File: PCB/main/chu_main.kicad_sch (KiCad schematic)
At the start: 83 parts, among them K1 Conn_01x01_Female, K10 Conn_01x01_Female, K11 Conn_01x01_Female, K12 Conn_01x01_Female, K13 Conn_01x01_Female, K14 Conn_01x01_Female, K15 Conn_01x01_Female, K16 Conn_01x01_Female, K17 Conn_01x01_Female, K18 Conn_01x01_Female, K19 Conn_01x01_Female, K2 Conn_01x01_Female, K20 Conn_01x01_Female, K21 Conn_01x01_Female, K22 Conn_01x01_Female, K23 Conn_01x01_Female, K24 Conn_01x01_Female, K25 Conn_01x01_Female, K26 Conn_01x01_Female, K27 Conn_01x01_Female, K28 Conn_01x01_Female, K29 Conn_01x01_Female, K3 Conn_01x01_Female, K30 Conn_01x01_Female, K31 Conn_01x01_Female, K32 Conn_01x01_Female, K4 Conn_01x01_Female, K5 Conn_01x01_Female, K6 Conn_01x01_Female, K7 Conn_01x01_Female, K8 Conn_01x01_Female, K9 Conn_01x01_Female, U1 Pico, U3 MPR121QR2_BOARD, U4 MPR121QR2_BOARD, U5 MPR121QR2_BOARD, U8 SN74LV1T34DBV

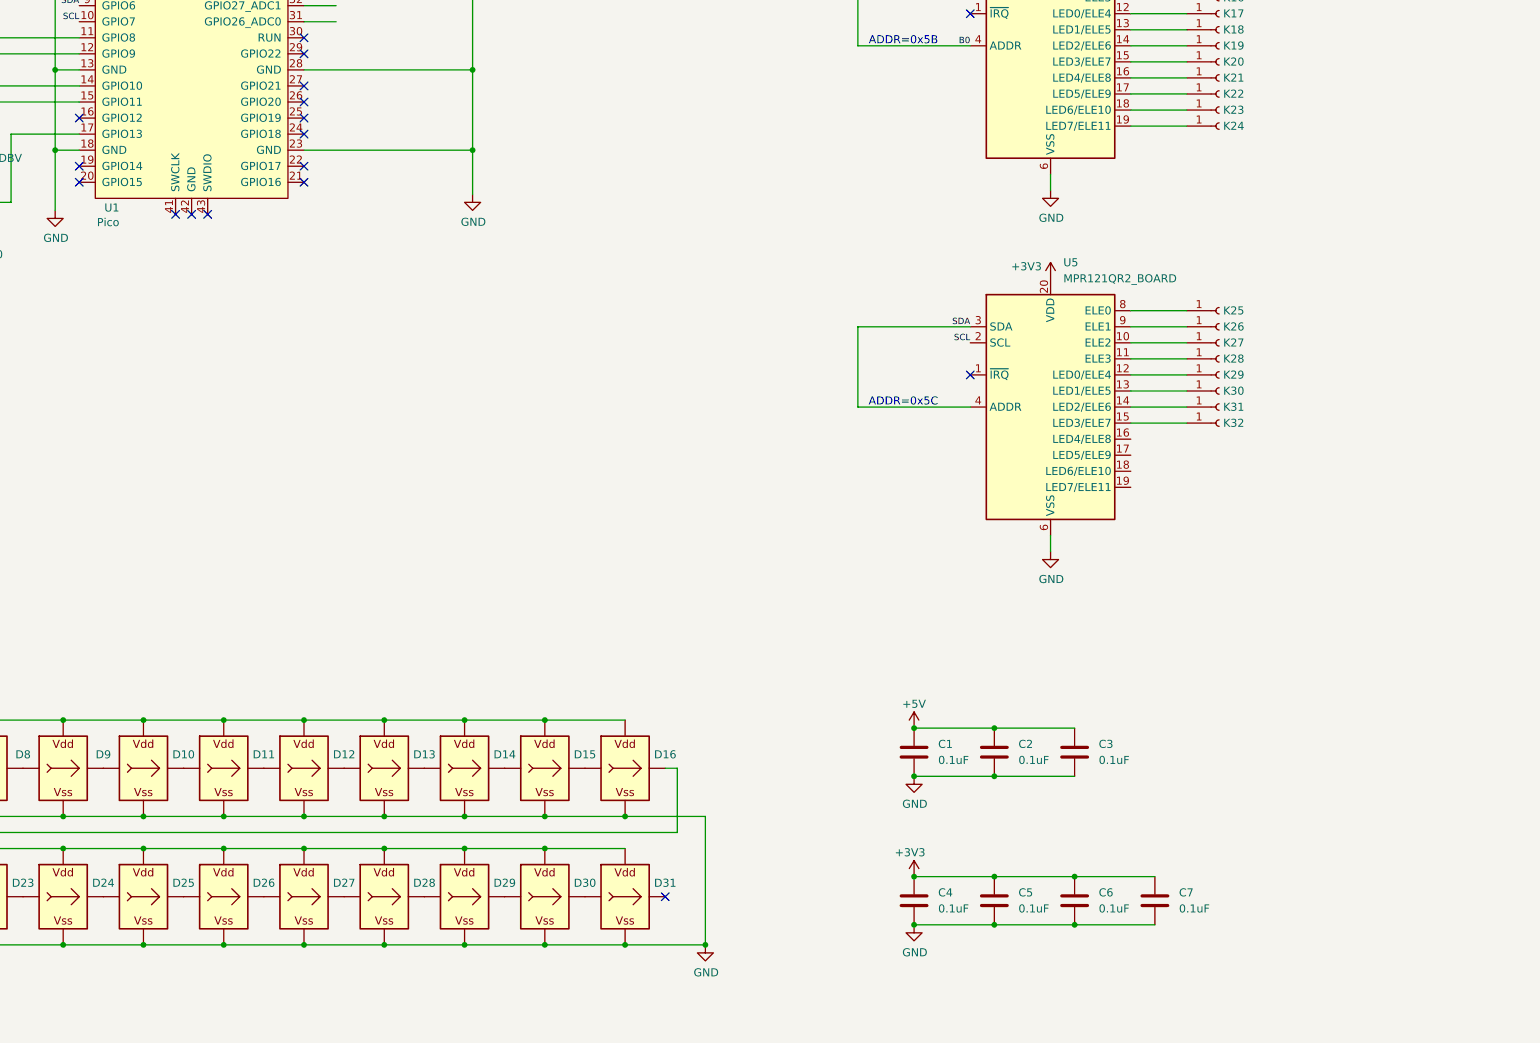
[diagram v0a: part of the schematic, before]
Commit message: Some updates (keypad, IR sensor firmware)
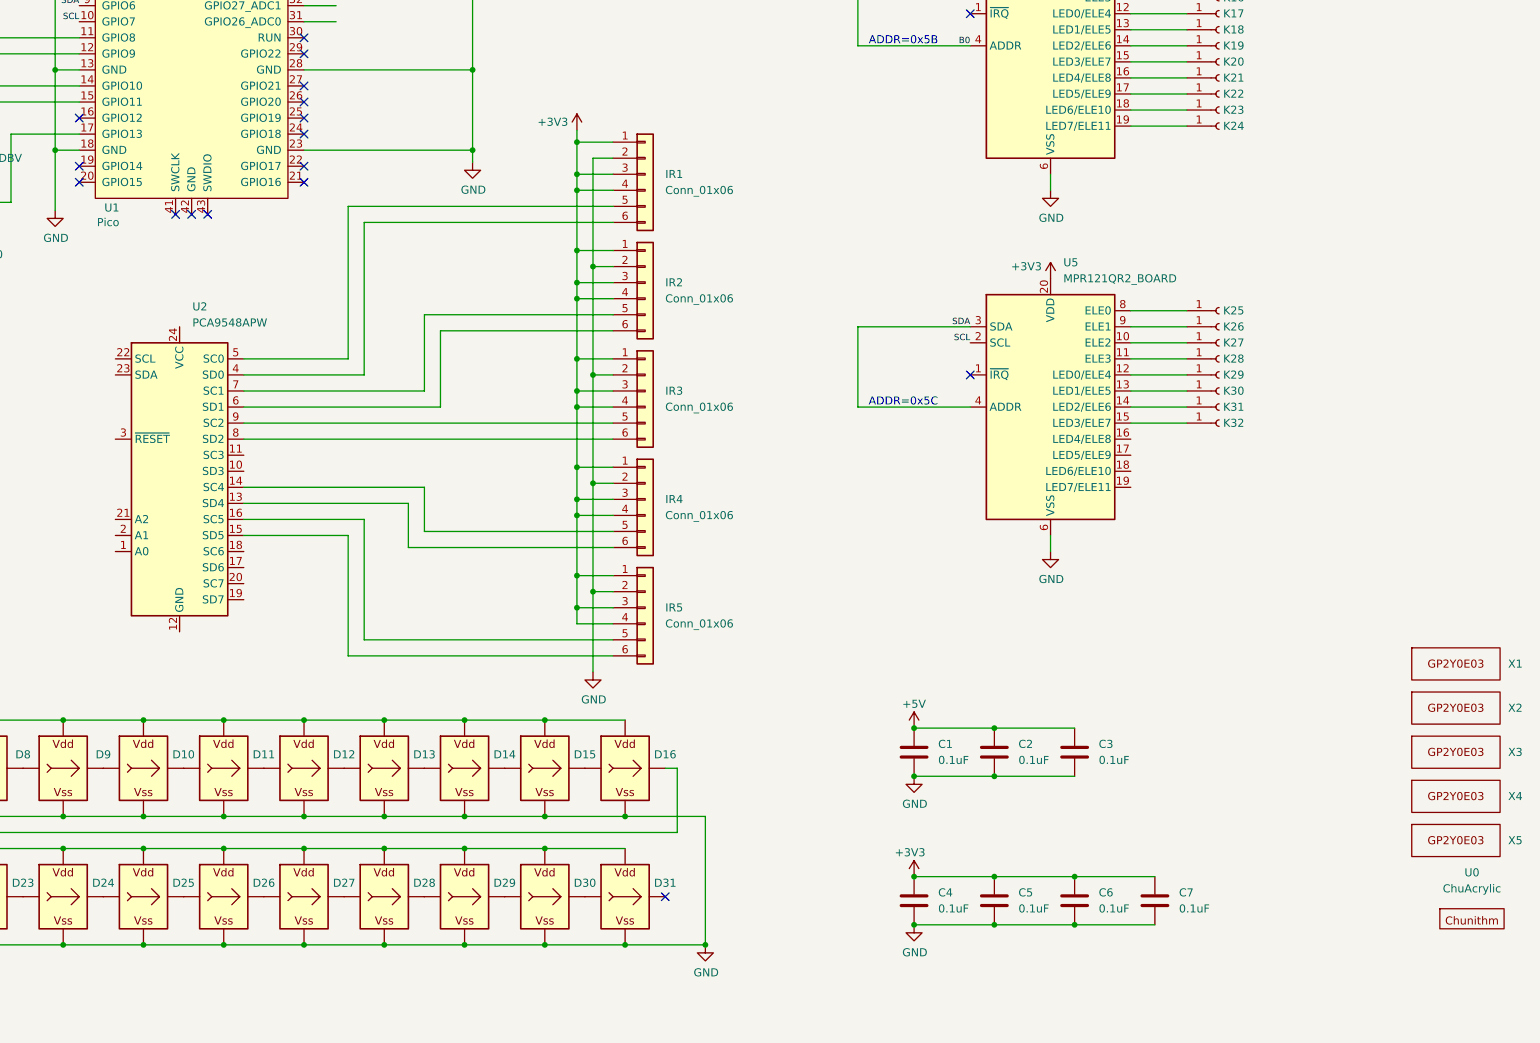
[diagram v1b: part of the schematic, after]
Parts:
- added IR1, IR2, IR3, IR4, IR5: Conn_01x06, chu_main:GP2Y0E03, symbol Connector_Generic:Conn_01x06
- added U0: ChuAcrylic, chu_main:ChuAcrylic, symbol chu_main:ChuAcrylic
- added U2: PCA9548APW, Package_SO:TSSOP-24_4.4x7.8mm_P0.65mm, symbol Interface_Expansion:PCA9548APW
- added X1, X2, X3, X4, X5: GP2Y0E03_REAL, chu_main:GP2Y0E03_REAL, symbol chu_main:GP2Y0E03_REAL
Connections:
- net +3V3: now also IR1.1 (Pin_1), IR1.3 (Pin_3), IR1.4 (Pin_4), IR2.1 (Pin_1), IR2.3 (Pin_3), IR2.4 (Pin_4), IR3.1 (Pin_1), IR3.3 (Pin_3), IR3.4 (Pin_4), IR4.1 (Pin_1), IR4.3 (Pin_3), IR4.4 (Pin_4), IR5.1 (Pin_1), IR5.3 (Pin_3), IR5.4 (Pin_4)
- net GND: now also IR1.2 (Pin_2), IR2.2 (Pin_2), IR3.2 (Pin_2), IR4.2 (Pin_2), IR5.2 (Pin_2)
- new net: IR4.5 (Pin_5), U2.14 (SC4)
- new net: IR4.6 (Pin_6), U2.13 (SD4)
- new net: IR1.5 (Pin_5), U2.5 (SC0)
- new net: IR1.6 (Pin_6), U2.4 (SD0)
- new net: IR2.5 (Pin_5), U2.7 (SC1)
- new net: IR2.6 (Pin_6), U2.6 (SD1)
- new net: IR3.5 (Pin_5), U2.9 (SC2)
- new net: IR3.6 (Pin_6), U2.8 (SD2)
- new net: IR5.5 (Pin_5), U2.16 (SC5)
- new net: IR5.6 (Pin_6), U2.15 (SD5)

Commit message: Layout progress 40%
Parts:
- added D32, D33, D34, D35, D36: WS2812B_Unified, chu_main:WS2812B-2835, symbol chu_main:WS2812B_Unified
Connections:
- net +5V: now also D32.V (VDD), D33.V (VDD), D34.V (VDD), D35.V (VDD), D36.V (VDD)
- net GND: now also D32.G (VSS), D33.G (VSS), D34.G (VSS), D35.G (VSS), D36.G (VSS)
- net at D31.O (Out): now also D32.I (In)
- new net: D32.O (Out), D33.I (In)
- new net: D34.O (Out), D35.I (In)
- new net: D35.O (Out), D36.I (In)
- new net: D33.O (Out), D34.I (In)

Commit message: Layoug progress 70%
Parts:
- added R10, R11, R12, R13, R4, R5, R6, R7, R8, R9: 4.7K, Resistor_SMD:R_0603_1608Metric, symbol Device:R_Small
- U1: footprint chu_main:RPi_Pico_SMD_Pins -> chu_main:RPi_Pico_SMD_Pins_Strip
- renumbered R20 to R1, R21 to R2, R4 to R3
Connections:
- net +3V3: now also U2.24 (VCC), R10.2, R11.2, R12.2, R13.2, R4.2, R5.2, R6.2, R7.2, R8.2, R9.2
- net GND: now also U2.1 (A0), U2.12 (GND), U2.2 (A1), U2.21 (A2)
- net SCL: now also U1.22 (GPIO17), U2.22 (SCL); no longer U1.10 (GPIO7)
- net SDA: now also U1.21 (GPIO16), U2.23 (SDA); no longer U1.9 (GPIO6)
- net at R3.2, U8.2 (A): now also U1.4 (GPIO2); no longer U1.17 (GPIO13)
- net at U1.25 (GPIO19): now also U2.3 (~{RESET})
- net SCL_2: now reaches U2.14 (SC4)
- net SCL_2: now also IR2.5 (Pin_5), R6.1; no longer IR4.5 (Pin_5)
- net SDA_2: now reaches U2.13 (SD4)
- net SDA_2: now also IR2.6 (Pin_6), R7.1; no longer IR4.6 (Pin_6)
- net SCL_1: now reaches IR1.5 (Pin_5)
- net SCL_1: now also U2.16 (SC5), R4.1; no longer U2.5 (SC0)
- net SDA_1: now reaches IR1.6 (Pin_6)
- net SDA_1: now also U2.15 (SD5), R5.1; no longer U2.4 (SD0)
- net SCL_5: now reaches U2.7 (SC1)
- net SCL_5: now also IR5.5 (Pin_5), R12.1; no longer IR2.5 (Pin_5)
- net SDA_5: now reaches U2.6 (SD1)
- net SDA_5: now also IR5.6 (Pin_6), R13.1; no longer IR2.6 (Pin_6)
- net SCL_3: now reaches IR3.5 (Pin_5)
- net SCL_3: now also U2.5 (SC0), R8.1; no longer U2.9 (SC2)
- net SDA_3: now reaches IR3.6 (Pin_6)
- net SDA_3: now also U2.4 (SD0), R9.1; no longer U2.8 (SD2)
- new net SCL_4: IR4.5 (Pin_5), R10.1, U2.9 (SC2)
- new net SDA_4: IR4.6 (Pin_6), R11.1, U2.8 (SD2)
- no-connect marks 25 -> 41
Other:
- moved on the sheet: IR1, IR2, IR3, IR4, IR5, R3, U1, U8

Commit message: PCB v1 done
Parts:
- added C6: 0.1uF, Capacitor_SMD:C_0603_1608Metric_Pad1.08x0.95mm_HandSolder, symbol Device:C
- renumbered C6 to C8
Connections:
- net B0 is gone; now on net +3V3: U4.4 (ADDR)
- net +3V3: no longer C4.1, C5.1, C7.1
- net +5V: now also C4.1, C5.1, C7.1, C6.1
- net GND: now also C6.2
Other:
- moved on the sheet: C1, C2, C3, C4, C5, C8

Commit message: PCB v1.1 (LED footprint update)
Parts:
- D32, D33, D34, D35, D36: footprint chu_main:WS2812B-2835 -> chu_main:WS2812B-4020
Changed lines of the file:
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@@
       (effects (font (size 1.27 1.27)) hide)
     )
-    (property "Footprint" "chu_main:WS2812B-2835" (id 2) (at 83.82 269.24 0)
+    (property "Footprint" "chu_main:WS2812B-4020" (id 2) (at 83.82 269.24 0)
       (effects (font (size 1.27 1.27)) (justify left top) hide)
     )
@@
       (effects (font (size 1.27 1.27)) hide)
     )
-    (property "Footprint" "chu_main:WS2812B-2835" (id 2) (at 121.92 269.24 0)
+    (property "Footprint" "chu_main:WS2812B-4020" (id 2) (at 121.92 269.24 0)
       (effects (font (size 1.27 1.27)) (justify left top) hide)
     )
@@
       (effects (font (size 1.27 1.27)) hide)
     )
-    (property "Footprint" "chu_main:WS2812B-2835" (id 2) (at 109.22 269.24 0)
+    (property "Footprint" "chu_main:WS2812B-4020" (id 2) (at 109.22 269.24 0)
       (effects (font (size 1.27 1.27)) (justify left top) hide)
     )
@@
       (effects (font (size 1.27 1.27)) hide)
     )
-    (property "Footprint" "chu_main:WS2812B-2835" (id 2) (at 96.52 269.24 0)
+    (property "Footprint" "chu_main:WS2812B-4020" (id 2) (at 96.52 269.24 0)
       (effects (font (size 1.27 1.27)) (justify left top) hide)
     )
@@
       (effects (font (size 1.27 1.27)) hide)
     )
-    (property "Footprint" "chu_main:WS2812B-2835" (id 2) (at 134.62 269.24 0)
+    (property "Footprint" "chu_main:WS2812B-4020" (id 2) (at 134.62 269.24 0)
       (effects (font (size 1.27 1.27)) (justify left top) hide)
     )
@@
     )
     (path "/0601a6ad-0bb7-4dea-8b69-576e319947e8"
-      (reference "D32") (unit 1) (value "WS2812B_Unified") (footprint "chu_main:WS2812B-2835")
+      (reference "D32") (unit 1) (value "WS2812B_Unified") (footprint "chu_main:WS2812B-4020")
     )
     (path "/748713f3-186a-410a-9525-4caea40c2977"
-      (reference "D33") (unit 1) (value "WS2812B_Unified") (footprint "chu_main:WS2812B-2835")
+      (reference "D33") (unit 1) (value "WS2812B_Unified") (footprint "chu_main:WS2812B-4020")
     )
     (path "/6dae0991-cb3e-47fa-a605-c2da04657d64"
-      (reference "D34") (unit 1) (value "WS2812B_Unified") (footprint "chu_main:WS2812B-2835")
+      (reference "D34") (unit 1) (value "WS2812B_Unified") (footprint "chu_main:WS2812B-4020")
     )
     (path "/22b824d1-9964-4065-ad53-8a225029207b"
-      (reference "D35") (unit 1) (value "WS2812B_Unified") (footprint "chu_main:WS2812B-2835")
+      (reference "D35") (unit 1) (value "WS2812B_Unified") (footprint "chu_main:WS2812B-4020")
     )
     (path "/f9638a2d-254e-4d1b-82c0-7c7b0aa8cf89"
-      (reference "D36") (unit 1) (value "WS2812B_Unified") (footprint "chu_main:WS2812B-2835")
+      (reference "D36") (unit 1) (value "WS2812B_Unified") (footprint "chu_main:WS2812B-4020")
     )
     (path "/5da28692-0cd4-4544-9250-22252cbda908"

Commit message: Finetune PCB and CAD files
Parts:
- K10, K12, K14, K16, K18, K2, K20, K22, K24, K26, K28, K30, K32, K4, K6, K8: footprint chu_main:ChuKeyScrews -> chu_main:ChuKey
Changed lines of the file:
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@@
       (effects (font (size 1.27 1.27)) (justify left) hide)
     )
-    (property "Footprint" "chu_main:ChuKeyScrews" (id 2) (at 354.33 162.56 0)
+    (property "Footprint" "chu_main:ChuKey" (id 2) (at 354.33 162.56 0)
       (effects (font (size 1.27 1.27)) hide)
     )
@@
       (effects (font (size 1.27 1.27)) (justify left) hide)
     )
-    (property "Footprint" "chu_main:ChuKeyScrews" (id 2) (at 354.33 90.17 0)
+    (property "Footprint" "chu_main:ChuKey" (id 2) (at 354.33 90.17 0)
       (effects (font (size 1.27 1.27)) hide)
     )
@@
       (effects (font (size 1.27 1.27)) (justify left) hide)
     )
-    (property "Footprint" "chu_main:ChuKeyScrews" (id 2) (at 354.33 157.48 0)
+    (property "Footprint" "chu_main:ChuKey" (id 2) (at 354.33 157.48 0)
       (effects (font (size 1.27 1.27)) hide)
     )
@@
       (effects (font (size 1.27 1.27)) (justify left) hide)
     )
-    (property "Footprint" "chu_main:ChuKeyScrews" (id 2) (at 354.33 43.18 0)
+    (property "Footprint" "chu_main:ChuKey" (id 2) (at 354.33 43.18 0)
       (effects (font (size 1.27 1.27)) hide)
     )
@@
       (effects (font (size 1.27 1.27)) (justify left) hide)
     )
-    (property "Footprint" "chu_main:ChuKeyScrews" (id 2) (at 354.33 53.34 0)
+    (property "Footprint" "chu_main:ChuKey" (id 2) (at 354.33 53.34 0)
       (effects (font (size 1.27 1.27)) hide)
     )
@@
       (effects (font (size 1.27 1.27)) (justify left) hide)
     )
-    (property "Footprint" "chu_main:ChuKeyScrews" (id 2) (at 354.33 105.41 0)
+    (property "Footprint" "chu_main:ChuKey" (id 2) (at 354.33 105.41 0)
       (effects (font (size 1.27 1.27)) hide)
     )
@@
       (effects (font (size 1.27 1.27)) (justify left) hide)
     )
-    (property "Footprint" "chu_main:ChuKeyScrews" (id 2) (at 354.33 110.49 0)
+    (property "Footprint" "chu_main:ChuKey" (id 2) (at 354.33 110.49 0)
       (effects (font (size 1.27 1.27)) hide)
     )
@@
       (effects (font (size 1.27 1.27)) (justify left) hide)
     )
-    (property "Footprint" "chu_main:ChuKeyScrews" (id 2) (at 354.33 95.25 0)
+    (property "Footprint" "chu_main:ChuKey" (id 2) (at 354.33 95.25 0)
       (effects (font (size 1.27 1.27)) hide)
     )
@@
       (effects (font (size 1.27 1.27)) (justify left) hide)
     )
-    (property "Footprint" "chu_main:ChuKeyScrews" (id 2) (at 354.33 115.57 0)
+    (property "Footprint" "chu_main:ChuKey" (id 2) (at 354.33 115.57 0)
       (effects (font (size 1.27 1.27)) hide)
     )
@@
       (effects (font (size 1.27 1.27)) (justify left) hide)
     )
-    (property "Footprint" "chu_main:ChuKeyScrews" (id 2) (at 354.33 147.32 0)
+    (property "Footprint" "chu_main:ChuKey" (id 2) (at 354.33 147.32 0)
       (effects (font (size 1.27 1.27)) hide)
     )
@@
       (effects (font (size 1.27 1.27)) (justify left) hide)
     )
-    (property "Footprint" "chu_main:ChuKeyScrews" (id 2) (at 354.33 48.26 0)
+    (property "Footprint" "chu_main:ChuKey" (id 2) (at 354.33 48.26 0)
       (effects (font (size 1.27 1.27)) hide)
     )
@@
       (effects (font (size 1.27 1.27)) (justify left) hide)
     )
-    (property "Footprint" "chu_main:ChuKeyScrews" (id 2) (at 354.33 58.42 0)
+    (property "Footprint" "chu_main:ChuKey" (id 2) (at 354.33 58.42 0)
       (effects (font (size 1.27 1.27)) hide)
     )
@@
       (effects (font (size 1.27 1.27)) (justify left) hide)
     )
-    (property "Footprint" "chu_main:ChuKeyScrews" (id 2) (at 354.33 38.1 0)
+    (property "Footprint" "chu_main:ChuKey" (id 2) (at 354.33 38.1 0)
       (effects (font (size 1.27 1.27)) hide)
     )
@@
       (effects (font (size 1.27 1.27)) (justify left) hide)
     )
-    (property "Footprint" "chu_main:ChuKeyScrews" (id 2) (at 354.33 152.4 0)
+    (property "Footprint" "chu_main:ChuKey" (id 2) (at 354.33 152.4 0)
       (effects (font (size 1.27 1.27)) hide)
     )
@@
       (effects (font (size 1.27 1.27)) (justify left) hide)
     )
-    (property "Footprint" "chu_main:ChuKeyScrews" (id 2) (at 354.33 33.02 0)
+    (property "Footprint" "chu_main:ChuKey" (id 2) (at 354.33 33.02 0)
       (effects (font (size 1.27 1.27)) hide)
     )
@@
       (effects (font (size 1.27 1.27)) (justify left) hide)
     )
-    (property "Footprint" "chu_main:ChuKeyScrews" (id 2) (at 354.33 100.33 0)
+    (property "Footprint" "chu_main:ChuKey" (id 2) (at 354.33 100.33 0)
       (effects (font (size 1.27 1.27)) hide)
     )
@@
     )
     (path "/f9c41c5b-098b-4d5a-9976-ba6515a2ec7a"
-      (reference "K2") (unit 1) (value "Conn_01x01_Female") (footprint "chu_main:ChuKeyScrews")
+      (reference "K2") (unit 1) (value "Conn_01x01_Female") (footprint "chu_main:ChuKey")
     )
     (path "/08d85abb-3237-4d72-99f4-57092b02965c"
@@
     )
     (path "/df2d39c2-3ca5-4c87-97fa-12314841d0a0"
-      (reference "K4") (unit 1) (value "Conn_01x01_Female") (footprint "chu_main:ChuKeyScrews")
+      (reference "K4") (unit 1) (value "Conn_01x01_Female") (footprint "chu_main:ChuKey")
     )
     (path "/6ecbd99d-c2ce-4143-a99b-e8bcd2a7a013"
@@
     )
     (path "/4d878ce4-aae5-4362-b40c-c0ea29c8c9a4"
-      (reference "K6") (unit 1) (value "Conn_01x01_Female") (footprint "chu_main:ChuKeyScrews")
+      (reference "K6") (unit 1) (value "Conn_01x01_Female") (footprint "chu_main:ChuKey")
     )
     (path "/282b3b7f-4888-4ba1-8e3e-f750677d4343"
@@
     )
     (path "/c72f957e-5817-4166-8b43-d130f38d215d"
-      (reference "K8") (unit 1) (value "Conn_01x01_Female") (footprint "chu_main:ChuKeyScrews")
+      (reference "K8") (unit 1) (value "Conn_01x01_Female") (footprint "chu_main:ChuKey")
     )
     (path "/8eded052-2713-4c3d-8ebb-70994d2a49eb"
@@
     )
     (path "/79a4aff7-a5e2-4b7e-bb09-cf0dd022f771"
-      (reference "K10") (unit 1) (value "Conn_01x01_Female") (footprint "chu_main:ChuKeyScrews")
+      (reference "K10") (unit 1) (value "Conn_01x01_Female") (footprint "chu_main:ChuKey")
     )
     (path "/0563fcc7-e713-4f2d-9e87-2634364fb680"
@@
     )
     (path "/db4705d9-b3d2-49a4-96f3-33f3ee5db3c5"
-      (reference "K12") (unit 1) (value "Conn_01x01_Female") (footprint "chu_main:ChuKeyScrews")
+      (reference "K12") (unit 1) (value "Conn_01x01_Female") (footprint "chu_main:ChuKey")
     )
     (path "/fdd4bd59-1d65-42a6-b5bf-d786dc261db6"
@@
     )
     (path "/1cc33a48-faf2-4585-867a-a271a201d1c5"
-      (reference "K14") (unit 1) (value "Conn_01x01_Female") (footprint "chu_main:ChuKeyScrews")
+      (reference "K14") (unit 1) (value "Conn_01x01_Female") (footprint "chu_main:ChuKey")
     )
     (path "/551e7bff-6472-460c-adbb-2baecd766975"
@@
     )
     (path "/a6efa1f1-0c09-4f74-9948-95d685f056fa"
-      (reference "K16") (unit 1) (value "Conn_01x01_Female") (footprint "chu_main:ChuKeyScrews")
+      (reference "K16") (unit 1) (value "Conn_01x01_Female") (footprint "chu_main:ChuKey")
     )
     (path "/7fcaf0bc-9ab1-4c53-91fc-cd181af52a2c"
@@
     )
     (path "/fb2d01ff-dfa5-4ffd-b72f-0ed114023612"
-      (reference "K18") (unit 1) (value "Conn_01x01_Female") (footprint "chu_main:ChuKeyScrews")
+      (reference "K18") (unit 1) (value "Conn_01x01_Female") (footprint "chu_main:ChuKey")
     )
     (path "/47a29468-d763-49d8-a905-041dfd2b0fdb"
@@
     )
     (path "/8324a555-6f53-4c15-aa91-91ec35339cac"
-      (reference "K20") (unit 1) (value "Conn_01x01_Female") (footprint "chu_main:ChuKeyScrews")
+      (reference "K20") (unit 1) (value "Conn_01x01_Female") (footprint "chu_main:ChuKey")
     )
     (path "/f7103f9a-bdc4-45f5-add5-83a57c590782"
@@
     )
     (path "/9ac68718-a1f9-42bb-ab42-ac43d3637d9a"
-      (reference "K22") (unit 1) (value "Conn_01x01_Female") (footprint "chu_main:ChuKeyScrews")
+      (reference "K22") (unit 1) (value "Conn_01x01_Female") (footprint "chu_main:ChuKey")
     )
     (path "/70b72b6d-13c0-49b6-9606-488d841a2a1e"
@@
     )
     (path "/ae98f63d-97f8-4350-916b-711df88aa422"
-      (reference "K24") (unit 1) (value "Conn_01x01_Female") (footprint "chu_main:ChuKeyScrews")
+      (reference "K24") (unit 1) (value "Conn_01x01_Female") (footprint "chu_main:ChuKey")
     )
     (path "/9dffab08-f394-41c2-8837-8cc9e3f1bf44"
@@
     )
     (path "/bed81a25-aad1-400c-b41d-73f476c42ab9"
-      (reference "K26") (unit 1) (value "Conn_01x01_Female") (footprint "chu_main:ChuKeyScrews")
+      (reference "K26") (unit 1) (value "Conn_01x01_Female") (footprint "chu_main:ChuKey")
     )
     (path "/40517cf5-e968-448a-8be5-e06b125a310d"
@@
     )
     (path "/f5feeb96-188a-4208-8596-e178a6729411"
-      (reference "K28") (unit 1) (value "Conn_01x01_Female") (footprint "chu_main:ChuKeyScrews")
+      (reference "K28") (unit 1) (value "Conn_01x01_Female") (footprint "chu_main:ChuKey")
     )
     (path "/1d6a95ed-c55c-4902-989c-d4dae393eaf1"
@@
     )
     (path "/2380a383-dc0e-4aaf-a99f-306c0cad5767"
-      (reference "K30") (unit 1) (value "Conn_01x01_Female") (footprint "chu_main:ChuKeyScrews")
+      (reference "K30") (unit 1) (value "Conn_01x01_Female") (footprint "chu_main:ChuKey")
     )
     (path "/305da800-82ed-44e8-8e92-294aaad464d8"
@@
     )
     (path "/12267c2c-3011-4948-8756-07bf389ce661"
-      (reference "K32") (unit 1) (value "Conn_01x01_Female") (footprint "chu_main:ChuKeyScrews")
+      (reference "K32") (unit 1) (value "Conn_01x01_Female") (footprint "chu_main:ChuKey")
     )
     (path "/00000000-0000-0000-0000-000060fbdf0c"
